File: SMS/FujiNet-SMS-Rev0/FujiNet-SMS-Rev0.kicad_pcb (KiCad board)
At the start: 6 copper layers, 100 x 93 mm, 134 parts, among them J1 SMS_Cart_Edge_50, J2 USB-C, J3 microSD, J4 DBG UART, Q1 2N7002, Q2 AO3401A, SW1 S3_RST, SW2 RESET, SW3 S3_BOOT, SW4 BOOTSEL, U1 ESP32-S3-WROOM-1-N16R8, U10 AS6C4008-55TIN, U11 74HCT00, U12 74HCT14, U13 74HCT27, U2 CP2102N-A02-GQFN28, U3 UMH3N, U4 RP2354B, U5 AP63203WU, U6 AP2112K-3.3, U7 AS6C4008-55TIN, U8 74HCT10, U9 74HCT27, Y1 12MHz

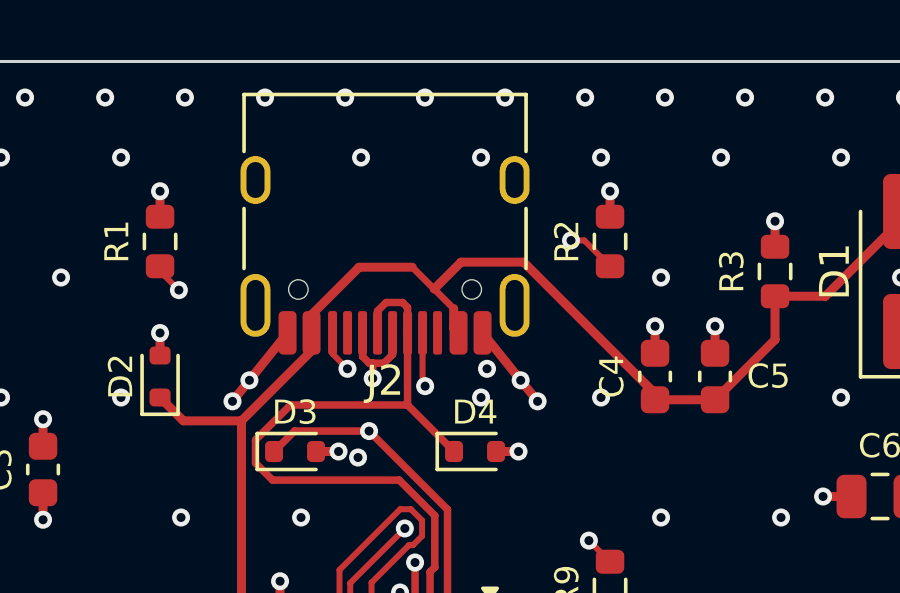
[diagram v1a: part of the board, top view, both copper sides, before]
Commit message: SMS Rev0: fix the microSD / USB-C alignment (J2 to the board edge, 3D models)
The same defect as NES Rev0: every cart copies the same HRO USB-C and SOFNG
TF-015 footprints and set_models.py rows.

- J2's shell face sat 1.35 mm inside the top edge, where a plug's overmold
  meets the PCB before the plug mates. HRO's recommended layout puts the
  edge at footprint y +3.19 (face 0.46 mm past it): J2 moves (128, 37) ->
  (128, 35.2). tools/usbc_to_edge.py, no re-route: the VBUS / D- ties move
  with J2, eight 1.8 mm F.Cu stubs join the new pad centres to the old
  ones, two edge-row GND stitching vias under the new front slots go.
  The VBUS exit east would have cut the rear shield slot and starved its
  F.Cu thermal (1 spoke): the CC2 via beside it moves 0.44 mm east onto its
  own bend, and VBUS drops at x 134 onto its original 45 degree line to
  C4. Front silk past the edge dropped; a Dwgs.User line marks HRO's edge.
- J2's 3D model: offset (0, -1.045, 0), not (0, +1.42, 0) (KiCad applies
  it after the rotation; the LCSC origin is the front shield legs).
- J3's 3D model: offset (-0.9, -5.5, 0), not (0, 0, 0) (the LCSC origin
  is the card centre on the peg line). J3's copper and position unchanged.
- case-spec: the USB-C is at x 128 (it said 126).

KiCad DRC at every severity with schematic parity on the saved fills:
0 / 0 / 0. check_vias, check_plane_shorts (both zips), check_gerbers and
check_fab clean. Drill changes: J2's slots and pegs, the removed vias, the
moved CC2 via; the CPLs change J2's Y only.

Co-Authored-By: Claude Opus 5.5 <noreply@anthropic.com>
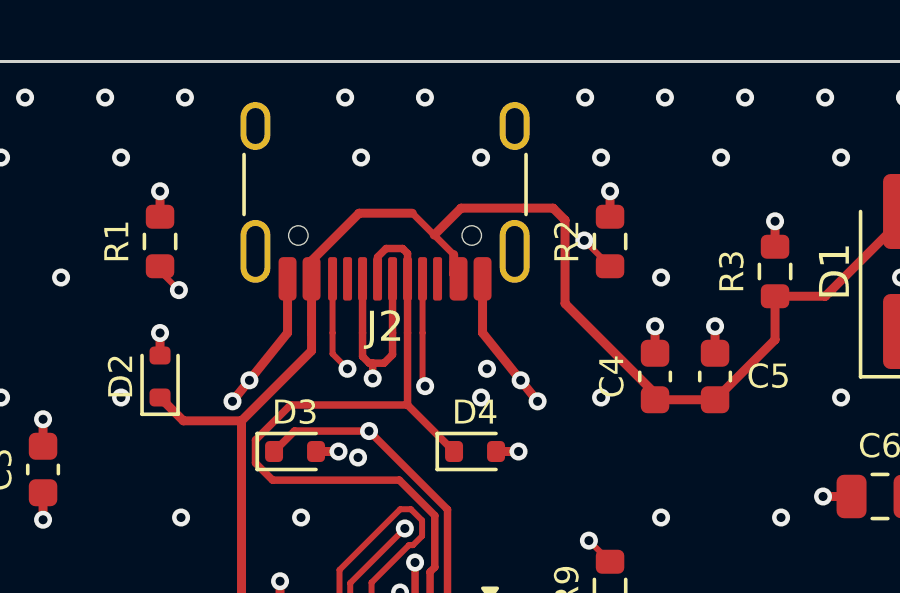
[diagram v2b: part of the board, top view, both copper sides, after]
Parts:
- moved J2 1.80 mm to (128.0, 35.2)
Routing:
- net VBUS: track 101.7 -> 105.9 mm
- net GND: track 140.1 -> 143.7 mm, vias 390 -> 388
- net /usb/UBRG_DP: track 15.8 -> 19.4 mm
- net /usb/UBRG_DM: track 23.9 -> 25.7 mm
- net /usb/CC1: track 12.6 -> 14.4 mm
- net /usb/CC2: track 13.6 -> 15.0 mm
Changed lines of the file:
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@@
 		(model "${KIPRJMOD}/3d/TF-015.step"
 			(offset
-				(xyz 0 0 0)
+				(xyz -0.9 -5.5 0)
 			)
 			(scale
@@
 	(footprint "FujiNet-SMS:USB_C_Receptacle_HRO_TYPE-C-31-M-12"
 		(layer "F.Cu")
-		(at 128 37 180)
-		(descr "USB Type-C receptacle for USB 2.0 and PD, http://www.krhro.com/uploads/soft/180320/1-1P320120243.pdf")
+		(at 128 35.2 180)
+		(descr "USB Type-C receptacle for USB 2.0 and PD, http://www.krhro.com/uploads/soft/180320/1-1P320120243.pdf; PCB edge at y 3.19 (HRO recommended layout: 5.79 mm in front of the pegs), the shell face overhangs it by 0.46 mm")
 		(tags "usb usb-c 2.0 pd")
 		(property "Reference" "J2"
@@
 		(duplicate_pad_numbers_are_jumpers no)
 		(fp_line
-			(start 4.7 2)
-			(end 4.7 3.9)
-			(stroke
-				(width 0.12)
-				(type solid)
-			)
-			(layer "F.SilkS")
-		)
-		(fp_line
 			(start 4.7 -1.9)
 			(end 4.7 0.1)
@@
 		)
 		(fp_line
-			(start -4.7 3.9)
-			(end 4.7 3.9)
-			(stroke
-				(width 0.12)
-				(type solid)
-			)
-			(layer "F.SilkS")
-		)
-		(fp_line
-			(start -4.7 2)
-			(end -4.7 3.9)
+			(start -4.7 -1.9)
+			(end -4.7 0.1)
 			(stroke
 				(width 0.12)
@@
 		)
 		(fp_line
-			(start -4.7 -1.9)
-			(end -4.7 0.1)
+			(start -5.32 3.19)
+			(end 5.32 3.19)
 			(stroke
-				(width 0.12)
-				(type solid)
+				(width 0.1)
+				(type dash)
 			)
-			(layer "F.SilkS")
+			(layer "Dwgs.User")
 		)
 		(fp_line
@@
 		(model "${KIPRJMOD}/3d/USB-C_HRO_TYPE-C-31-M-12.step"
 			(offset
-				(xyz 0 1.42 0)
+				(xyz 0 -1.045 0)
 			)
 			(scale
@@
 	)
 	(segment
+		(start 131.25 39.245)
+		(end 131.25 41.045)
+		(width 0.3)
+		(layer "F.Cu")
+		(net "GND")
+	)
+	(segment
 		(start 69.5 72.375)
 		(end 70.551 73.032)
@@
 	)
 	(segment
+		(start 124.75 39.245)
+		(end 124.75 41.045)
+		(width 0.3)
+		(layer "F.Cu")
+		(net "GND")
+	)
+	(segment
 		(start 55 80.375)
 		(end 53.949 81.032)
@@
 	)
 	(via
-		(at 132 33.2)
-		(size 0.6)
-		(drill 0.3)
-		(layers "F.Cu" "B.Cu")
-		(locked yes)
-		(net "GND")
-	)
-	(via
 		(at 55.16 55.07)
 		(size 0.6)
@@
 	)
 	(via
-		(at 124 33.2)
-		(size 0.6)
-		(drill 0.3)
-		(layers "F.Cu" "B.Cu")
-		(locked yes)
-		(net "GND")
-	)
-	(via
 		(at 145.2 39.2)
 		(size 0.6)
@@
 	)
 	(segment
-		(start 134.1991 37.9655)
-		(end 134.6405 37.9655)
+		(start 126.25 39.245)
+		(end 126.25 41.045)
 		(width 0.2)
 		(layer "F.Cu")
@@
 	)
 	(via
-		(at 134.1991 37.9655)
+		(at 134.6405 37.9655)
 		(size 0.6)
 		(drill 0.3)
@@
 	)
 	(segment
-		(start 134.1991 37.9655)
+		(start 134.6405 37.9655)
 		(end 134.1991 39.8866)
 		(width 0.2)
@@
 	)
 	(segment
+		(start 134 40.0688)
+		(end 134 37.2883)
+		(width 0.3)
+		(layer "F.Cu")
+		(net "VBUS")
+	)
+	(segment
+		(start 133.6 36.8883)
+		(end 132.6195 36.8883)
+		(width 0.3)
+		(layer "F.Cu")
+		(net "VBUS")
+	)
+	(segment
 		(start 121.2779 43.9779)
 		(end 120.5 43.2)
@@
 	)
 	(segment
-		(start 142.675 39.825)
-		(end 145.5 37)
+		(start 137 43.0688)
+		(end 134 40.0688)
 		(width 0.3)
 		(layer "F.Cu")
@@
 	)
 	(segment
-		(start 130.2877 40.8827)
-		(end 130.45 41.045)
+		(start 142.675 39.825)
+		(end 145.5 37)
 		(width 0.3)
 		(layer "F.Cu")
@@
 	)
 	(segment
-		(start 141 39.825)
-		(end 142.675 39.825)
+		(start 130.2877 39.0827)
+		(end 130.45 39.245)
 		(width 0.3)
 		(layer "F.Cu")
@@
 	)
 	(segment
-		(start 137 43.0688)
-		(end 132.6195 38.6883)
+		(start 141 39.825)
+		(end 142.675 39.825)
 		(width 0.3)
 		(layer "F.Cu")
@@
 	)
 	(segment
-		(start 127.1363 38.8571)
-		(end 125.55 40.4434)
+		(start 127.1363 37.0571)
+		(end 125.55 38.6434)
 		(width 0.3)
 		(layer "F.Cu")
@@
 	)
 	(segment
-		(start 130.2877 40.2354)
-		(end 130.2877 40.8827)
+		(start 130.2877 38.4354)
+		(end 130.2877 39.0827)
 		(width 0.3)
 		(layer "F.Cu")
@@
 	)
 	(segment
+		(start 134 37.2883)
+		(end 133.6 36.8883)
+		(width 0.3)
+		(layer "F.Cu")
+		(net "VBUS")
+	)
+	(segment
 		(start 123.2155 43.9779)
 		(end 123.2155 57.0405)
@@
 	)
 	(segment
-		(start 128.9094 38.8571)
-		(end 129.6371 39.5848)
+		(start 128.9094 37.0571)
+		(end 129.6371 37.7848)
 		(width 0.225)
 		(layer "F.Cu")
@@
 	)
 	(segment
-		(start 129.6371 39.5848)
-		(end 130.2877 40.2354)
+		(start 129.6371 37.7848)
+		(end 130.2877 38.4354)
 		(width 0.225)
 		(layer "F.Cu")
@@
 	)
 	(segment
-		(start 132.6195 38.6883)
-		(end 130.5336 38.6883)
+		(start 132.6195 36.8883)
+		(end 130.5336 36.8883)
 		(width 0.3)
 		(layer "F.Cu")
@@
 	)
 	(segment
-		(start 125.55 40.4434)
-		(end 125.55 41.045)
+		(start 125.55 38.6434)
+		(end 125.55 39.245)
 		(width 0.3)
 		(layer "F.Cu")
@@
 	)
 	(segment
-		(start 130.5336 38.6883)
-		(end 129.6371 39.5848)
+		(start 130.5336 36.8883)
+		(end 129.6371 37.7848)
+		(width 0.3)
+		(layer "F.Cu")
+		(net "VBUS")
+	)
+	(segment
+		(start 125.55 39.245)
+		(end 125.55 41.045)
 		(width 0.3)
 		(layer "F.Cu")
@@
 	)
 	(segment
-		(start 128.9094 38.8571)
-		(end 127.1363 38.8571)
+		(start 128.9094 37.0571)
+		(end 127.1363 37.0571)
 		(width 0.3)
 		(layer "F.Cu")
@@
 	)
 	(segment
-		(start 128.75 40.1993)
-		(end 128.75 41.045)
+		(start 128.75 38.3993)
+		(end 128.75 39.245)
 		(width 0.25)
 		(layer "F.Cu")
@@
 	)
 	(segment
-		(start 127.75 41.045)
-		(end 127.75 40.3185)
+		(start 127.75 39.245)
+		(end 127.75 38.5185)
 		(width 0.25)
 		(layer "F.Cu")
@@
 	)
 	(segment
-		(start 127.75 40.3185)
-		(end 128.0344 40.0341)
+		(start 127.75 38.5185)
+		(end 128.0344 38.2341)
 		(width 0.25)
 		(layer "F.Cu")
@@
 	)
 	(segment
-		(start 128.0344 40.0341)
-		(end 128.5848 40.0341)
+		(start 128.0344 38.2341)
+		(end 128.5848 38.2341)
 		(width 0.25)
 		(layer "F.Cu")
@@
 	)
 	(segment
-		(start 128.5848 40.0341)
-		(end 128.75 40.1993)
+		(start 128.75 39.245)
+		(end 128.75 41.045)
+		(width 0.25)
+		(layer "F.Cu")
+		(net "/usb/UBRG_DM")
+	)
+	(segment
+		(start 128.5848 38.2341)
+		(end 128.75 38.3993)
 		(width 0.25)
 		(layer "F.Cu")
@@
 	)
 	(segment
+		(start 129.25 39.245)
+		(end 129.25 41.045)
+		(width 0.2)
+		(layer "F.Cu")
+		(net "/usb/CC1")
+	)
+	(segment
 		(start 129.25 42.7362)
 		(end 129.336 42.8222)
@@
 	)
 	(segment
+		(start 128.25 39.245)
+		(end 128.25 41.045)
+		(width 0.25)
+		(layer "F.Cu")
+		(net "/usb/UBRG_DP")
+	)
+	(segment
 		(start 127.4665 44.3186)
 		(end 124.9814 44.3186)
@@
 		(width 0.25)
 		(layer "F.Cu")
+		(net "/usb/UBRG_DP")
+	)
+	(segment
+		(start 127.25 39.245)
+		(end 127.25 41.045)
+		(width 0.25)
+		(layer "F.Cu")
